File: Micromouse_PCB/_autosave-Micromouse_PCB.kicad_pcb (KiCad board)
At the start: 2 copper layers, 104 parts, among them J1 Conn_01x06_MountingPin, J2 Conn_01x06_MountingPin, J3 ARM Cortex Debug, J4 Power, J5 ALARM PKLCS1212E, J6 USB-C, Q1 Q_NMOS_GSD, Q10 AA4040P3C-P22, Q11 Q_NMOS_GSD, Q12 Q_NMOS_GSD, Q13 AA4040P3C-P22, Q2 AA4040P3C-P22, Q3 Q_NMOS_GSD, Q4 AA4040P3C-P22, Q5 Q_NMOS_GSD, Q6 AA4040P3C-P22, Q7 Q_NMOS_GSD, Q8 AA4040P3C-P22, Q9 Q_NMOS_GSD, SW1 Slide switch, SW2 SW_Push, SW3 SW_Push, U1 STM32F105RCT6, U2 DRV8871DDA, U3 DRV8871DDA, U5 BMI088, U6 3V3_LDO AZ1117CH-3.3TRG1, U7 NCP1117-1.5_TO252, U8 USBLC6-2SC6, Y1 8MHz, OT32258MJBA4SL

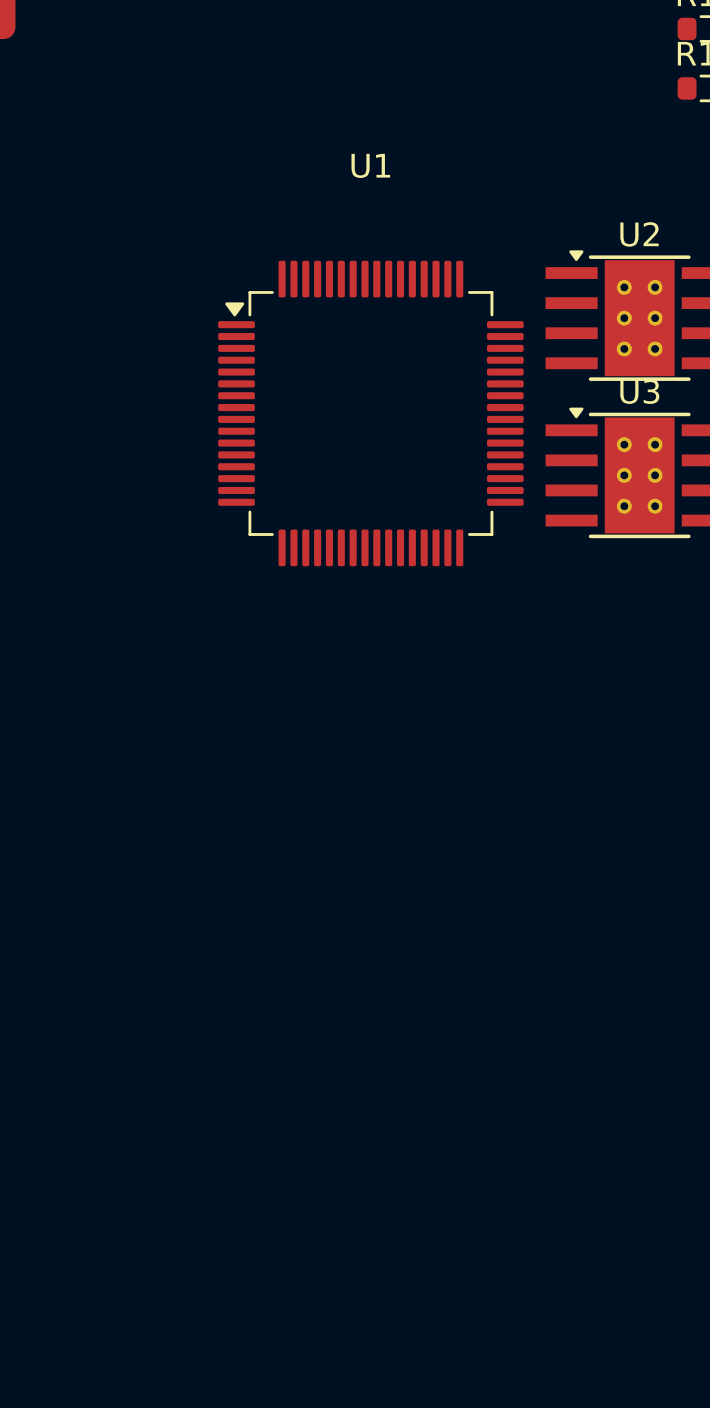
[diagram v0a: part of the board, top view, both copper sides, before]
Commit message: Schematic done
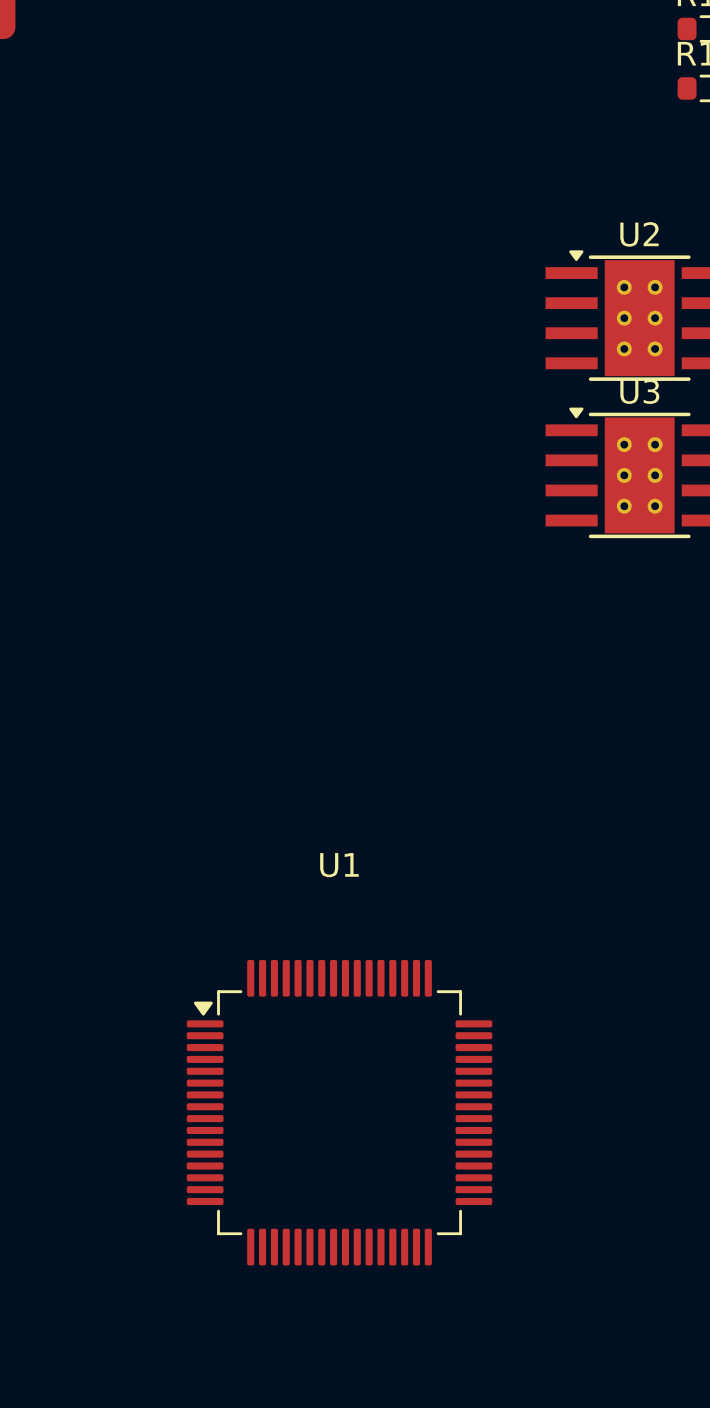
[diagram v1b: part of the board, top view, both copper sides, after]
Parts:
- moved U1 29.6 mm to (153.7, 95.3)
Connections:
- J1 pad 2: /PB7 -> /STM32F105RCT6/PB7
- J1 pad 3: /PB6 -> /STM32F105RCT6/PB6
- J2 pad 2: /PB3 -> /STM32F105RCT6/PB3
- J2 pad 3: /PA15 -> /STM32F105RCT6/PA15
- Q1 pad 1: /PA4 -> /STM32F105RCT6/PA4
- Q12 pad 1: /PA3 -> /STM32F105RCT6/PA3
- Q13 pad 2: /PA2 -> /STM32F105RCT6/PA2
- Q2 pad 2: /PA1 -> /STM32F105RCT6/PA1
- Q3 pad 1: /PA5 -> /STM32F105RCT6/PA5
- Q4 pad 2: /PA0 -> /STM32F105RCT6/PA0
- Q5 pad 1: /PA6 -> /STM32F105RCT6/PA6
- Q7 pad 1: /PA7 -> /STM32F105RCT6/PA7
- R1 pad 1: /PA4 -> /STM32F105RCT6/PA4
- R11 pad 1: /PA7 -> /STM32F105RCT6/PA7
- R16 pad 1: /PA2 -> /STM32F105RCT6/PA2
- R20 pad 1: /PA3 -> /STM32F105RCT6/PA3
- R3 pad 1: /PA1 -> /STM32F105RCT6/PA1
- R36 pad 2: /PA10 -> /STM32F105RCT6/PA10
- R37 pad 1: /PA10 -> /STM32F105RCT6/PA10
- R4 pad 1: /PA5 -> /STM32F105RCT6/PA5
- R6 pad 1: /PA0 -> /STM32F105RCT6/PA0
- R7 pad 1: /PA6 -> /STM32F105RCT6/PA6
- U5 pad 1: /PB2 -> /STM32F105RCT6/PB2
- U5 pad 10: /PB14 -> /STM32F105RCT6/PB14
- U5 pad 12: /PB0 -> /STM32F105RCT6/PB0
- U5 pad 14: /PB12 -> /STM32F105RCT6/PB12
- U5 pad 15: /PB14 -> /STM32F105RCT6/PB14
- U5 pad 16: /PB10 -> /STM32F105RCT6/PB10
- U5 pad 5: /PB11 -> /STM32F105RCT6/PB11
- U5 pad 8: /PB13 -> /STM32F105RCT6/PB13
- U5 pad 9: /PB15 -> /STM32F105RCT6/PB15
